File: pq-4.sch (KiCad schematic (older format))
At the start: 121 parts, among them IC1 M5218, IC2 M5218, IC3 M5218, IC4 M5218, IC5 M5218, J1 Conn_01x07_Male, J2 Conn_01x10_Male, Q1 2SK184-GR, Q2 2SC3378-GR, Q3 C2458-GR, Q4 C2458-GR, Q5 2SC3378-GR, Q6 2SC3378-GR, Q7 2SK118-Y, Q8 2SK118-Y, Q9 2SC3378-GR, SW1 SW_Push

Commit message: Minor improvements.
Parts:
- C15, C18, C2, C23, C24, C27, C29, C30, C31, C32, C33, C4, C5, C6: footprint Capacitor_THT:CP_Radial_D4.0mm_P2.00mm -> Capactor_w:CP_Radial_D4.0mm_P5.08mm
- HIGH1: renamed from RV2; symbol Device:R_POT_Dual_Separate -> pq-4-pots:R_POT_Triple_Separate
- HIGH1: value 100k -> 50k; symbol Device:R_POT -> pq-4-pots:R_POT_Triple_Separate; Resistance (none) -> 100k
- LP1: renamed from PRESENCE1; symbol Device:R_POT -> pq-4-pots:R_POT_wDetent_Dual_Separate
- LP1: renamed from LOW1; symbol Device:R_POT -> pq-4-pots:R_POT_wDetent_Dual_Separate
- MID1: renamed from RV3; symbol Device:R_POT_Dual_Separate -> pq-4-pots:R_POT_Triple_Separate
- MID1: renamed from MIDDLE1; value 100k -> 50k; symbol Device:R_POT -> pq-4-pots:R_POT_Triple_Separate; Resistance (none) -> 100k
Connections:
- net A: now also R31.2
- net A1: now also HIGH1.7, LP1.5, MID1.7; no longer HIGH1.1, LP1.1, MID1.1
- net A3: now also HIGH1.9, LP1.7, MID1.9; no longer HIGH1.3, LP1.3, MID1.3
- net C: now also HIGH1.10 (Central_tap), LP1.4 (Central_tap), LP1.8 (Central_tap), MID1.10 (Central_tap)
- net HL2: now also HIGH1.8; no longer HIGH1.2
- net LOW2: now also LP1.6; no longer LP1.2
- net ML2: now also MID1.8; no longer MID1.2
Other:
- note added: "Common central tap"
- note added: "Connectors to potentiometers board"
- note added: "Low/Presence concentric pot"
- note added: "On/Off toggle switch"
- moved on the sheet: C10, C16, C17, C21, C24, C25, C26, C27, C4, C5, C8, D1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

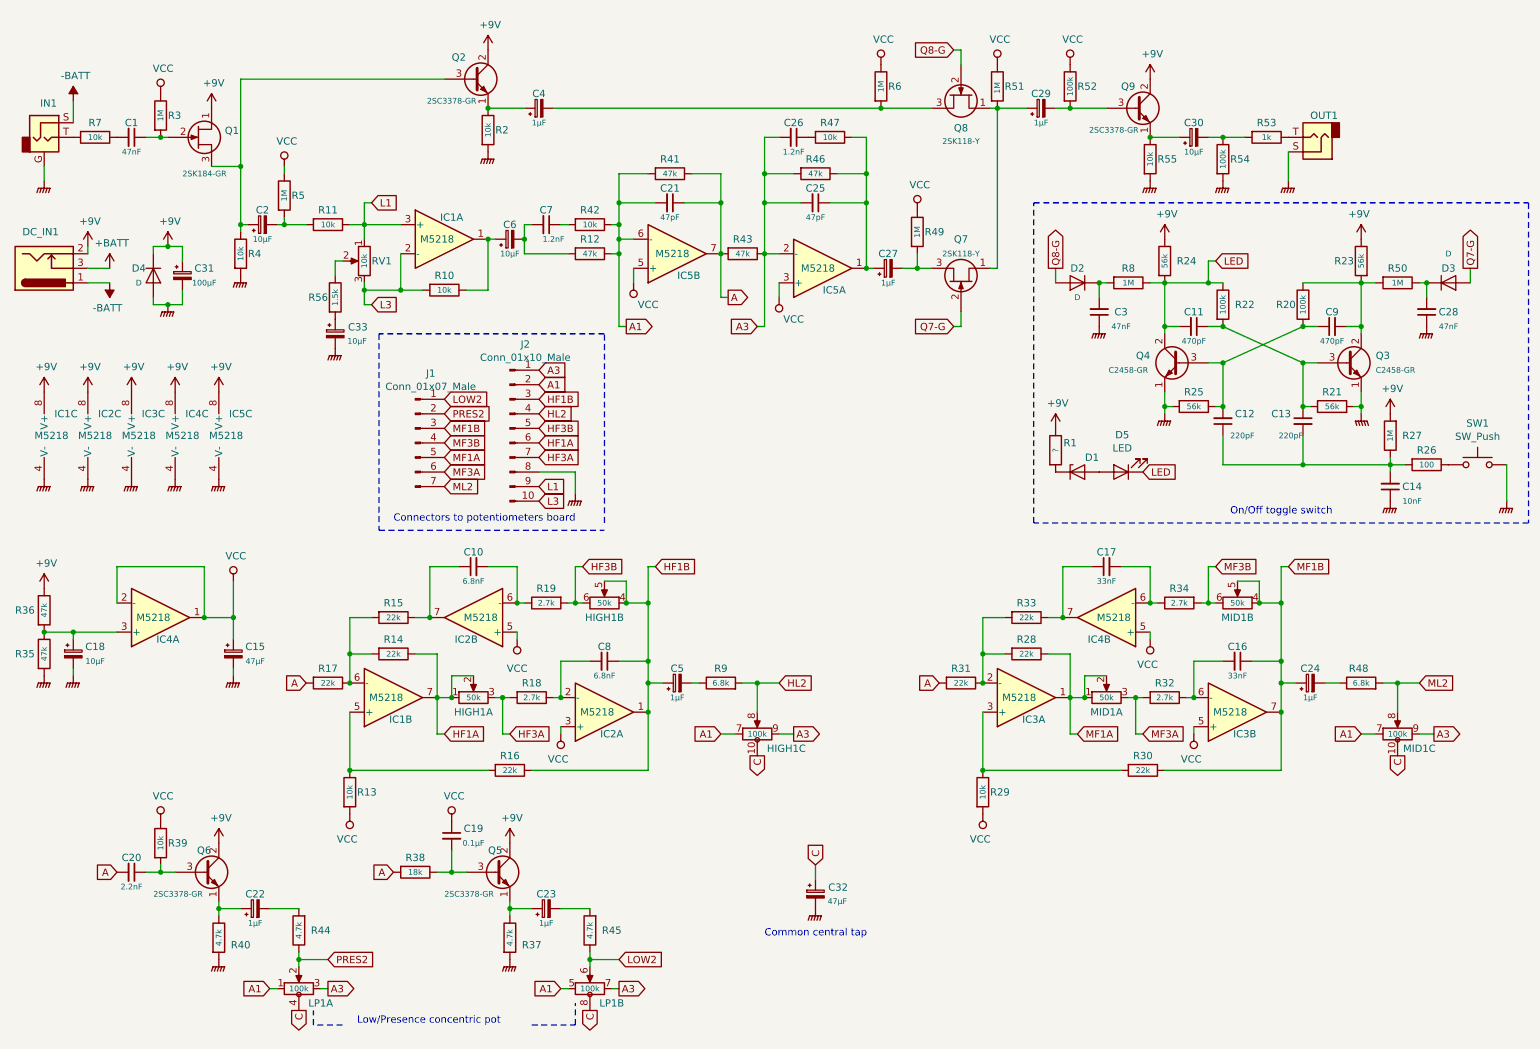
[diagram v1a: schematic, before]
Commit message: Updating schema layout.
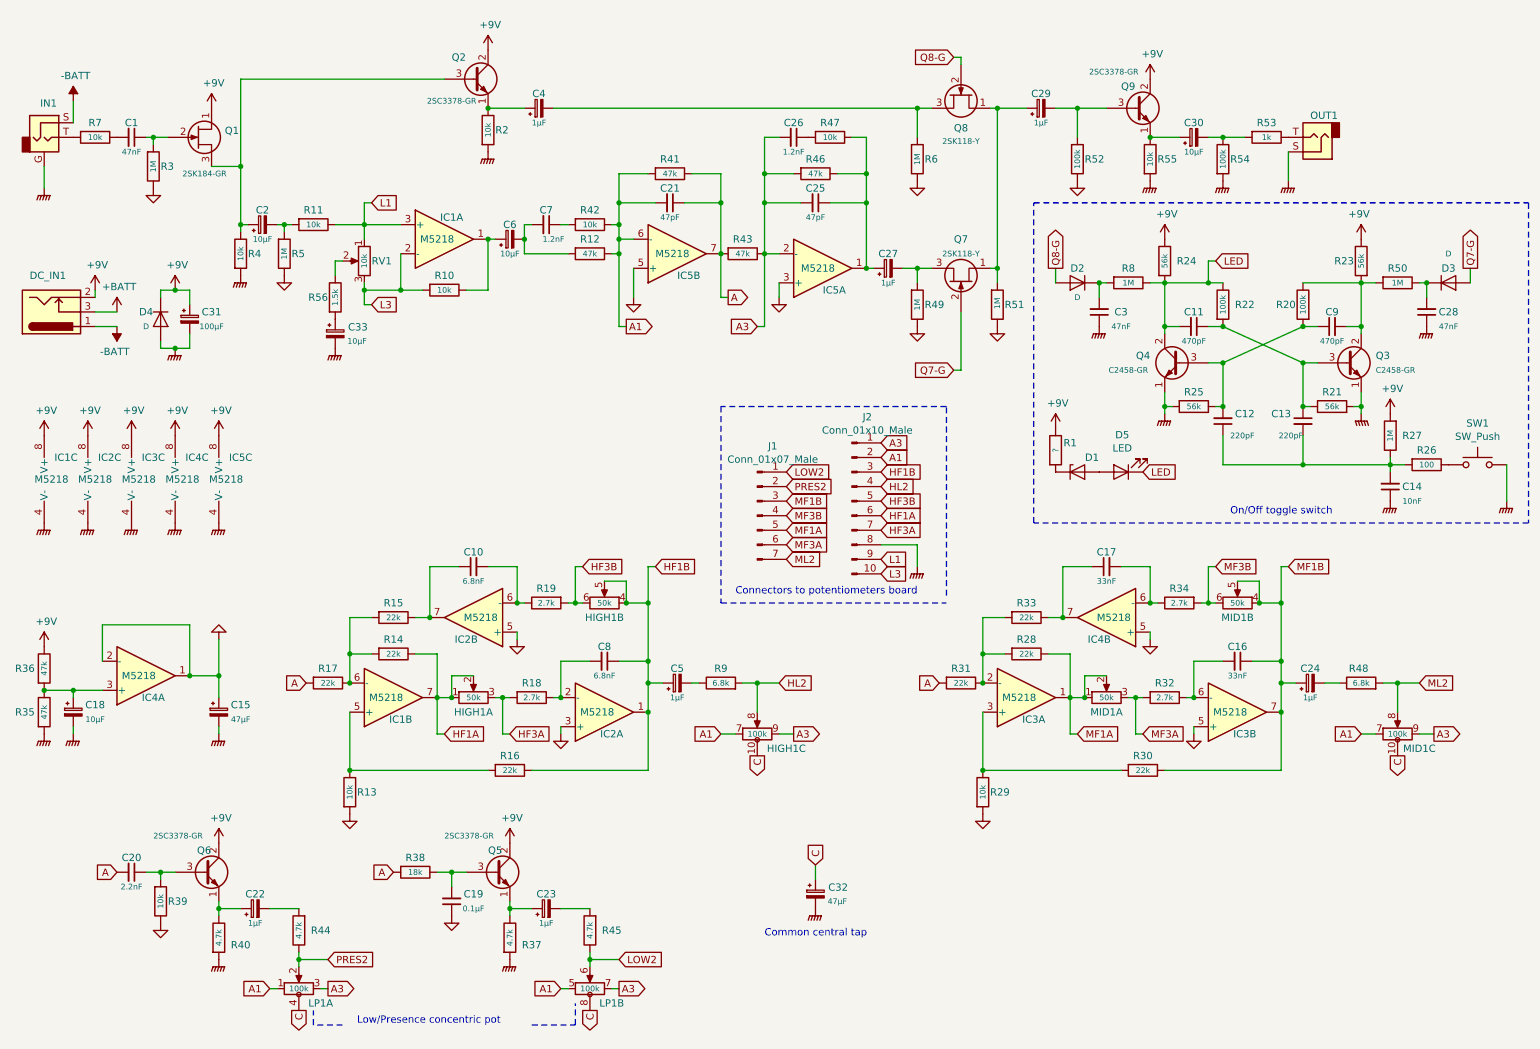
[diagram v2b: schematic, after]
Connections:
- net VCC renamed GNDA
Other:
- moved on the sheet: C15, C18, C19, C31, D4, DC_IN1, IC1C, IC2C, IC3C, IC4A, IC4C, IC5C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
